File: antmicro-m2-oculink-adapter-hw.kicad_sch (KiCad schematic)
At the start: 21 parts, among them J1 PCB-Edge_M.2_Key-M, J2 OCuLink_x4_Amphenol_G14A42121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

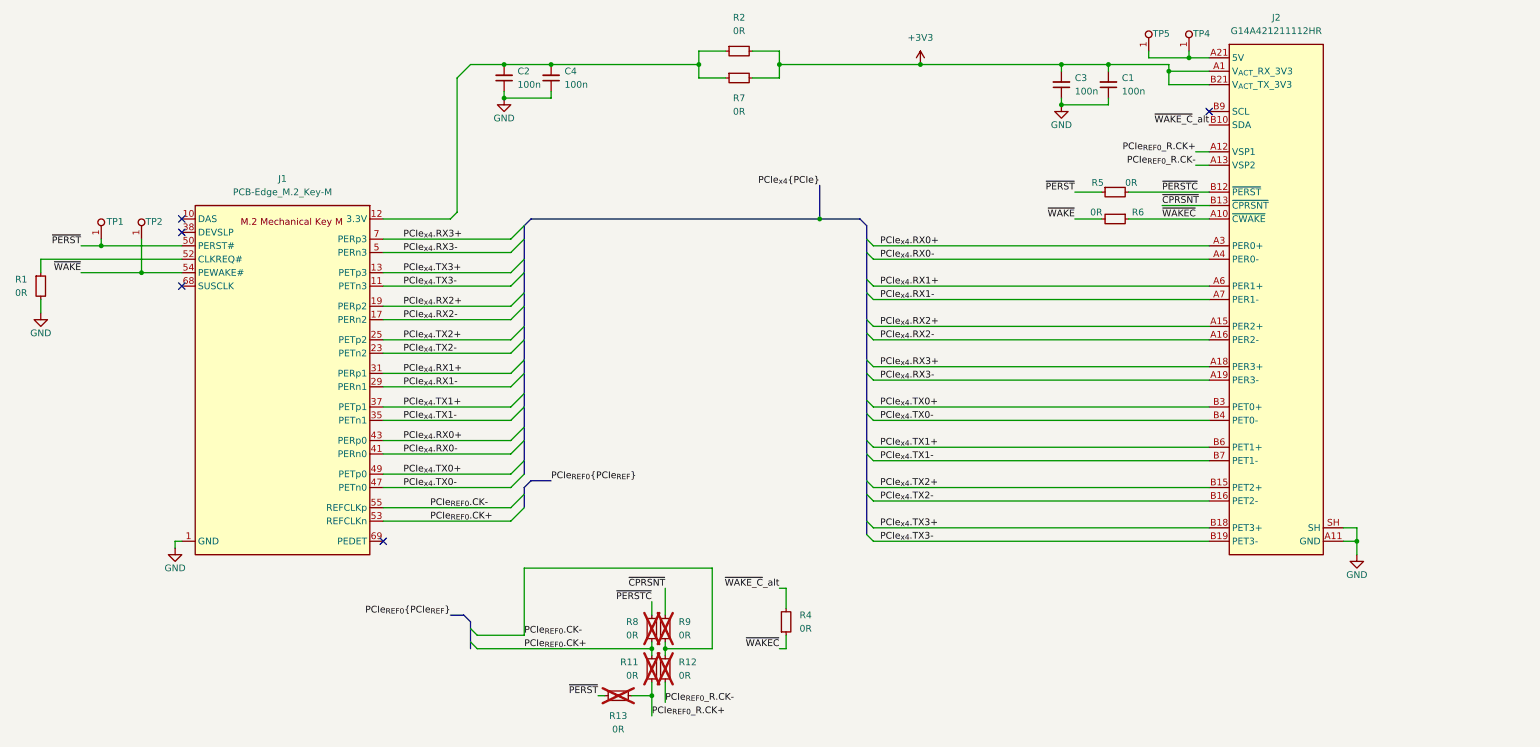
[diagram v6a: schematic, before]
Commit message: [#81131] Clean up drc
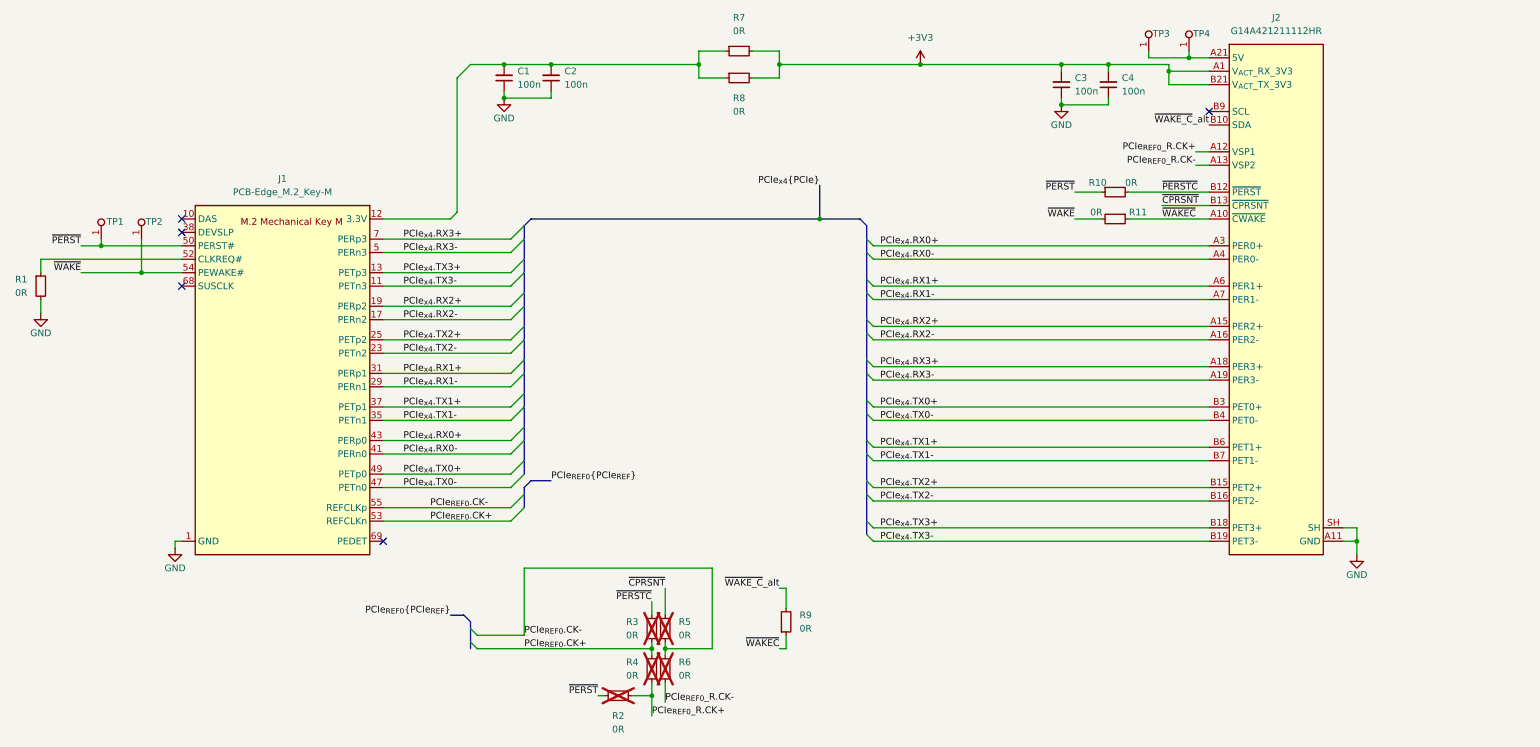
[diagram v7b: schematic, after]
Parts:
- renumbered C2 to C1, C4 to C2, C1 to C4, R5 to R10, R6 to R11, R13 to R2, R8 to R3, R11 to R4, R9 to R5, R12 to R6, R2 to R7, R7 to R8, R4 to R9, TP5 to TP3
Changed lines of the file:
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@@
 		(dnp no)
 		(fields_autoplaced yes)
-		(property "Reference" "C1"
+		(property "Reference" "C4"
 			(at 233.68 55.8736 90)
 			(effects
@@
 			(project ""
 				(path "/b9cca87b-aef2-493b-be4f-d9e02584eafa"
-					(reference "C1")
+					(reference "C4")
 					(unit 1)
 				)
@@
 		(dnp no)
 		(fields_autoplaced yes)
-		(property "Reference" "C2"
+		(property "Reference" "C1"
 			(at 119.38 54.6036 90)
 			(effects
@@
 			(project "antmicro-m2-oculink-adapter-hw"
 				(path "/b9cca87b-aef2-493b-be4f-d9e02584eafa"
-					(reference "C2")
+					(reference "C1")
 					(unit 1)
 				)
@@
 		(dnp no)
 		(fields_autoplaced yes)
-		(property "Reference" "C4"
+		(property "Reference" "C2"
 			(at 128.27 54.6036 90)
 			(effects
@@
 			(project "antmicro-m2-oculink-adapter-hw"
 				(path "/b9cca87b-aef2-493b-be4f-d9e02584eafa"
-					(reference "C4")
+					(reference "C2")
 					(unit 1)
 				)
@@
 		(dnp yes)
 		(fields_autoplaced yes)
-		(property "Reference" "R9"
+		(property "Reference" "R5"
 			(at 149.86 158.75 90)
 			(effects
@@
 			(project "antmicro-m2-oculink-adapter-hw"
 				(path "/b9cca87b-aef2-493b-be4f-d9e02584eafa"
-					(reference "R9")
+					(reference "R5")
 					(unit 1)
 				)
@@
 		(on_board yes)
 		(dnp no)
-		(property "Reference" "R5"
+		(property "Reference" "R10"
 			(at 229.108 75.692 0)
 			(effects
@@
 			(project "antmicro-m2-oculink-adapter-hw"
 				(path "/b9cca87b-aef2-493b-be4f-d9e02584eafa"
-					(reference "R5")
+					(reference "R10")
 					(unit 1)
 				)
@@
 		(dnp yes)
 		(fields_autoplaced yes)
-		(property "Reference" "R8"
+		(property "Reference" "R3"
 			(at 142.24 158.75 90)
 			(effects
@@
 			(project "antmicro-m2-oculink-adapter-hw"
 				(path "/b9cca87b-aef2-493b-be4f-d9e02584eafa"
-					(reference "R8")
+					(reference "R3")
 					(unit 1)
 				)
@@
 		(dnp yes)
 		(fields_autoplaced yes)
-		(property "Reference" "R12"
+		(property "Reference" "R6"
 			(at 149.86 166.37 90)
 			(effects
@@
 			(project "antmicro-m2-oculink-adapter-hw"
 				(path "/b9cca87b-aef2-493b-be4f-d9e02584eafa"
-					(reference "R12")
+					(reference "R6")
 					(unit 1)
 				)
@@
 		(on_board yes)
 		(dnp no)
-		(property "Reference" "#PWR04"
+		(property "Reference" "#PWR06"
 			(at 287.02 148.59 0)
 			(effects
@@
 			(project "antmicro-m2-oculink-adapter-hw"
 				(path "/b9cca87b-aef2-493b-be4f-d9e02584eafa"
-					(reference "#PWR04")
+					(reference "#PWR06")
 					(unit 1)
 				)
@@
 		(on_board yes)
 		(dnp no)
-		(property "Reference" "TP5"
+		(property "Reference" "TP3"
 			(at 239.522 47.498 90)
 			(effects
@@
 			(project "antmicro-m2-oculink-adapter-hw"
 				(path "/b9cca87b-aef2-493b-be4f-d9e02584eafa"
-					(reference "TP5")
+					(reference "TP3")
 					(unit 1)
 				)
@@
 		(on_board yes)
 		(dnp no)
-		(property "Reference" "R2"
+		(property "Reference" "R7"
 			(at 161.29 44.45 0)
 			(effects
@@
 			(project "antmicro-m2-oculink-adapter-hw"
 				(path "/b9cca87b-aef2-493b-be4f-d9e02584eafa"
-					(reference "R2")
+					(reference "R7")
 					(unit 1)
 				)
@@
 		(dnp no)
 		(fields_autoplaced yes)
-		(property "Reference" "#PWR03"
+		(property "Reference" "#PWR04"
 			(at 210.82 53.34 0)
 			(effects
@@
 			(project ""
 				(path "/b9cca87b-aef2-493b-be4f-d9e02584eafa"
-					(reference "#PWR03")
+					(reference "#PWR04")
 					(unit 1)
 				)
@@
 		(on_board yes)
 		(dnp no)
-		(property "Reference" "R6"
+		(property "Reference" "R11"
 			(at 236.728 81.28 0)
 			(effects
@@
 			(project "antmicro-m2-oculink-adapter-hw"
 				(path "/b9cca87b-aef2-493b-be4f-d9e02584eafa"
-					(reference "R6")
+					(reference "R11")
 					(unit 1)
 				)
@@
 		(on_board yes)
 		(dnp no)
-		(property "Reference" "#PWR06"
+		(property "Reference" "#PWR03"
 			(at 125.73 62.23 0)
 			(effects
@@
 			(project "antmicro-m2-oculink-adapter-hw"
 				(path "/b9cca87b-aef2-493b-be4f-d9e02584eafa"
-					(reference "#PWR06")
+					(reference "#PWR03")
 					(unit 1)
 				)
@@
 		(dnp yes)
 		(fields_autoplaced yes)
-		(property "Reference" "R11"
+		(property "Reference" "R4"
 			(at 142.24 166.37 90)
 			(effects
@@
 			(project "antmicro-m2-oculink-adapter-hw"
 				(path "/b9cca87b-aef2-493b-be4f-d9e02584eafa"
-					(reference "R11")
+					(reference "R4")
 					(unit 1)
 				)
@@
 		(dnp no)
 		(fields_autoplaced yes)
-		(property "Reference" "R4"
+		(property "Reference" "R9"
 			(at 172.72 157.48 90)
 			(effects
@@
 			(project "antmicro-m2-oculink-adapter-hw"
 				(path "/b9cca87b-aef2-493b-be4f-d9e02584eafa"
-					(reference "R4")
+					(reference "R9")
 					(unit 1)
 				)
@@
 		(dnp no)
 		(fields_autoplaced yes)
-		(property "Reference" "R7"
+		(property "Reference" "R8"
 			(at 161.29 59.69 0)
 			(effects
@@
 			(project "antmicro-m2-oculink-adapter-hw"
 				(path "/b9cca87b-aef2-493b-be4f-d9e02584eafa"
-					(reference "R7")
+					(reference "R8")
 					(unit 1)
 				)
@@
 		(dnp yes)
 		(fields_autoplaced yes)
-		(property "Reference" "R13"
+		(property "Reference" "R2"
 			(at 138.43 176.53 0)
 			(effects
@@
 			(project "antmicro-m2-oculink-adapter-hw"
 				(path "/b9cca87b-aef2-493b-be4f-d9e02584eafa"
-					(reference "R13")
+					(reference "R2")
 					(unit 1)
 				)

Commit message: [#81131] Fix schematic 3V3
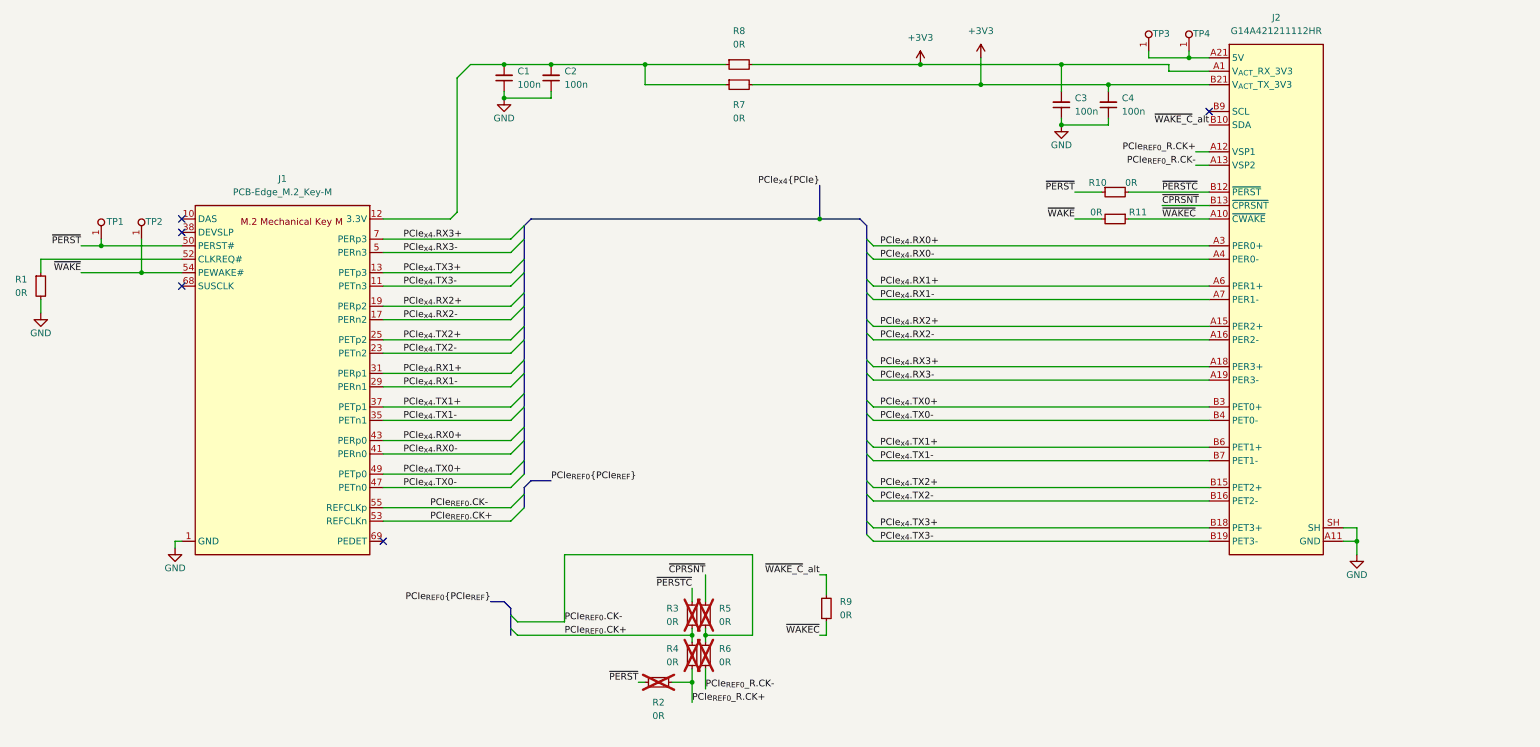
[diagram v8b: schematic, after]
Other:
- moved on the sheet: C3, C4, R2, R3, R4, R5, R6, R7, R8, R9
